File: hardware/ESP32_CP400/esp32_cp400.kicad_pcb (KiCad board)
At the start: 2 copper layers, 110 x 60 mm, 24 parts, among them J2 USB_A, J3 USB_A, J4 USB_A, J5 Micro_SD_Card, J6 Barrel_Jack, J7 DA15_Pins

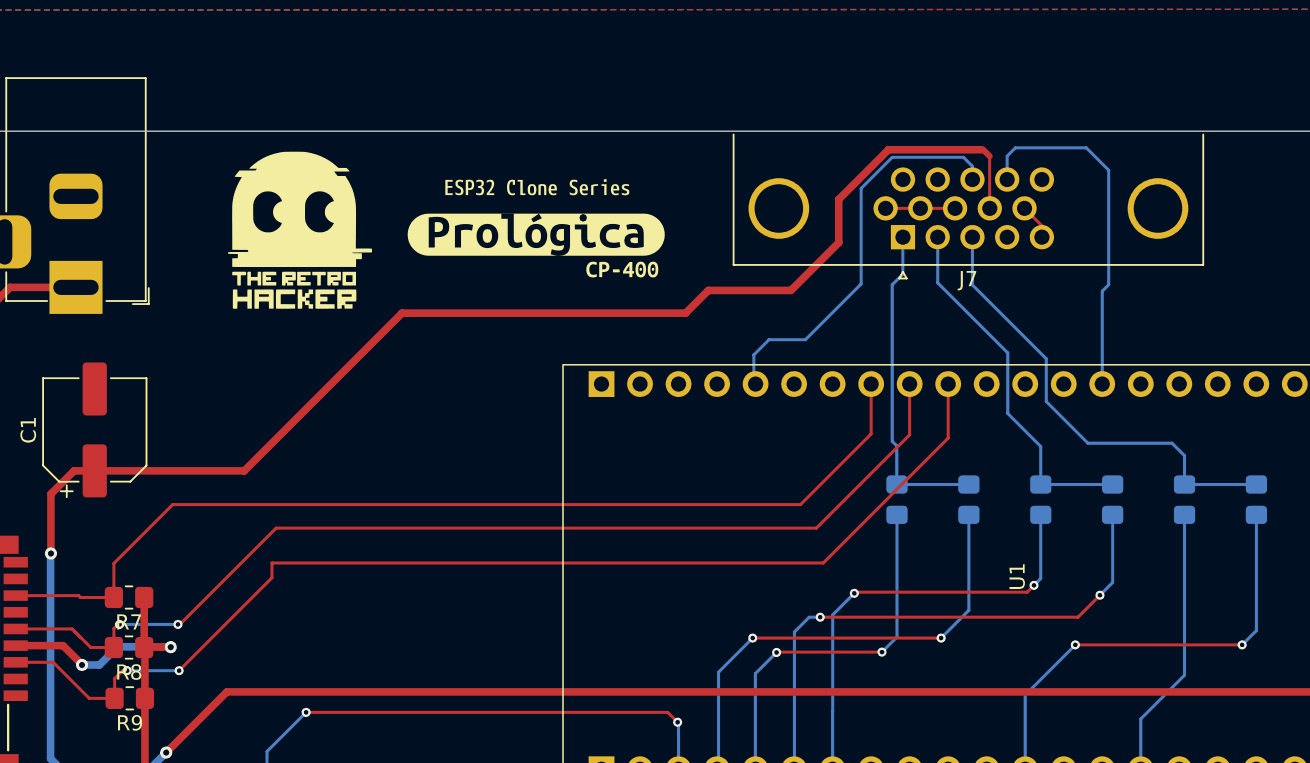
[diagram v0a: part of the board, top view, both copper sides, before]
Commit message: Add footprint for PJ-307 connector
- Created a new footprint file for the PJ-307 connector in the KiCad format.
- Included necessary attributes such as reference, value, and layer specifications.
- Defined pads for through-hole connections with appropriate sizes and drill specifications.
- Added graphical elements including lines and polygons for silk screen and fabrication layers.
- Provided a link to the datasheet for reference.
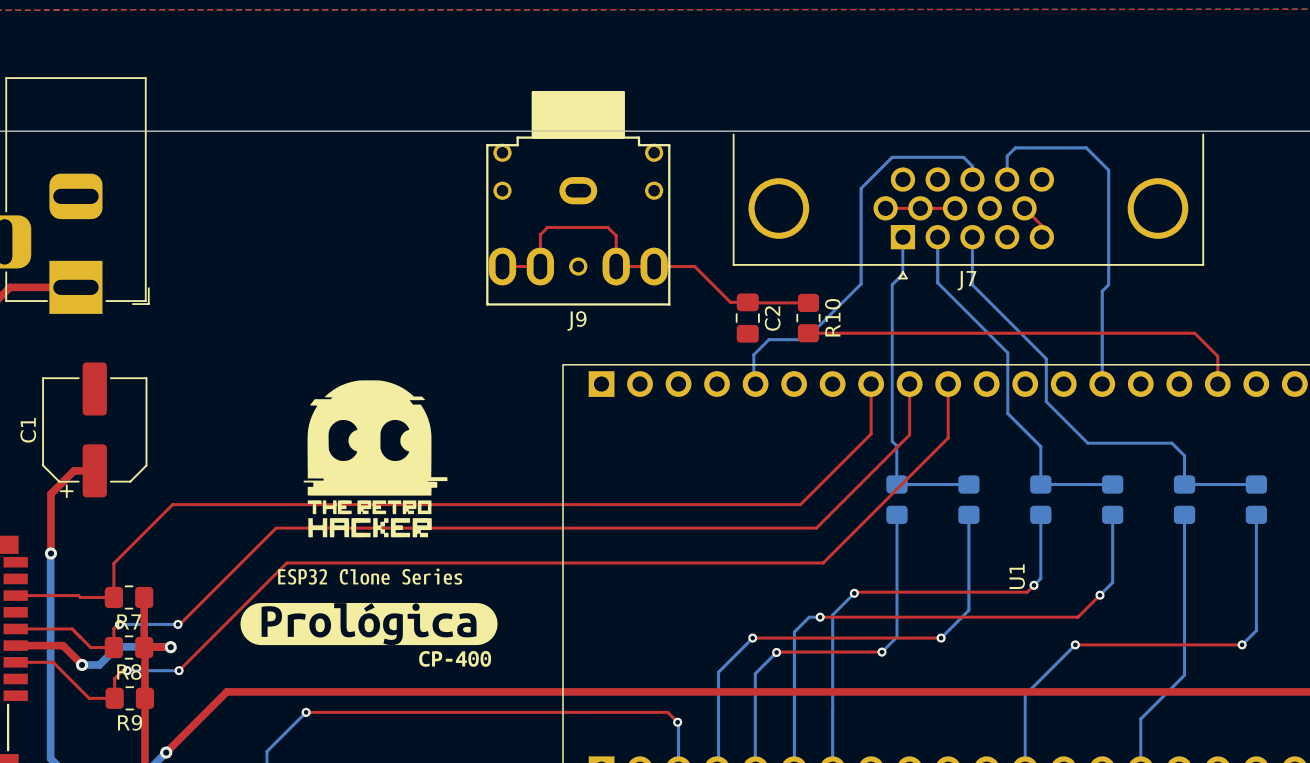
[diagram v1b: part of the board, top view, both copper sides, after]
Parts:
- added C2: C, Capacitor_SMD:C_0805_2012Metric_Pad1.18x1.45mm_HandSolder, F.Cu at (153.2, 72.3)
- added J9: AudioJack2_Ground, PJ307:PJ-307, F.Cu at (142.1, 66.9)
- added R10: 1k, Resistor_SMD:R_0805_2012Metric_Pad1.20x1.40mm_HandSolder, F.Cu at (157.2, 72.3)
- moved kibuzzard-6A32A222 27.9 mm to (133.9, 94.8)
- moved kibuzzard-6A32A22E 27.9 mm to (128.3, 92.5)
- moved kibuzzard-6A32A25A 27.9 mm to (128.3, 89.4)
- moved G*** 15.9 mm to (128.4, 82.0)
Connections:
- J7 pad 9: +5V -> unconnected-(J7-P9-Pad9)
- U1 pad 6: unconnected-(U1-IO47-Pad6) -> Net-(U1-IO47)
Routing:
- net +5V: track 200.4 -> 127.3 mm
- net Net-(U1-IO47): track 0.00 -> 29.5 mm
- net Net-(C2-Pad1): track 0.00 -> 25.7 mm
- net Net-(J5-CMD): track 74.5 -> 73.9 mm
